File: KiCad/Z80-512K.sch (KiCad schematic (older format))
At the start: 31 parts, among them J1 VBAT, J2 JTAG, J3 RC2014_BUS, J4 RC2014_EXT, U1 Z84C00, U2 SST39SF040, U3 AS6C4008, U4 ATF1504AS, U5 ADM693A, X1 7.3728MHz

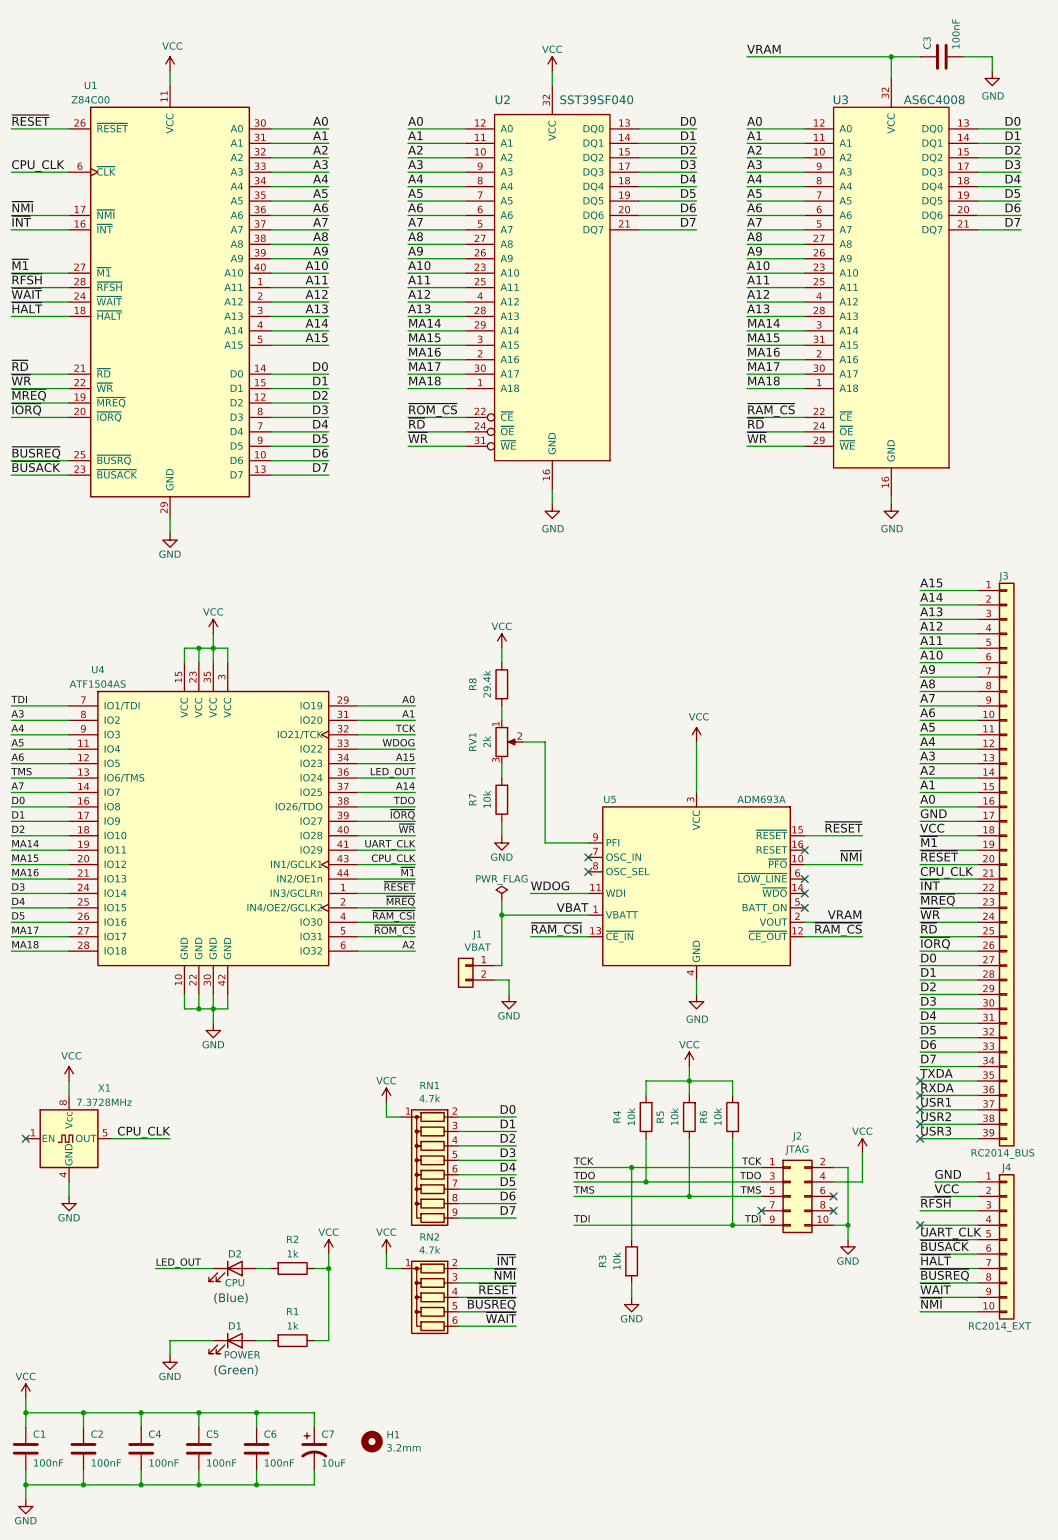
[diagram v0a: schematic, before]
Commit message: Update KiCad, gerber, and README for Version 1.1
Signed-off-by: Sergey Kiselev <skiselev@gmail.com>
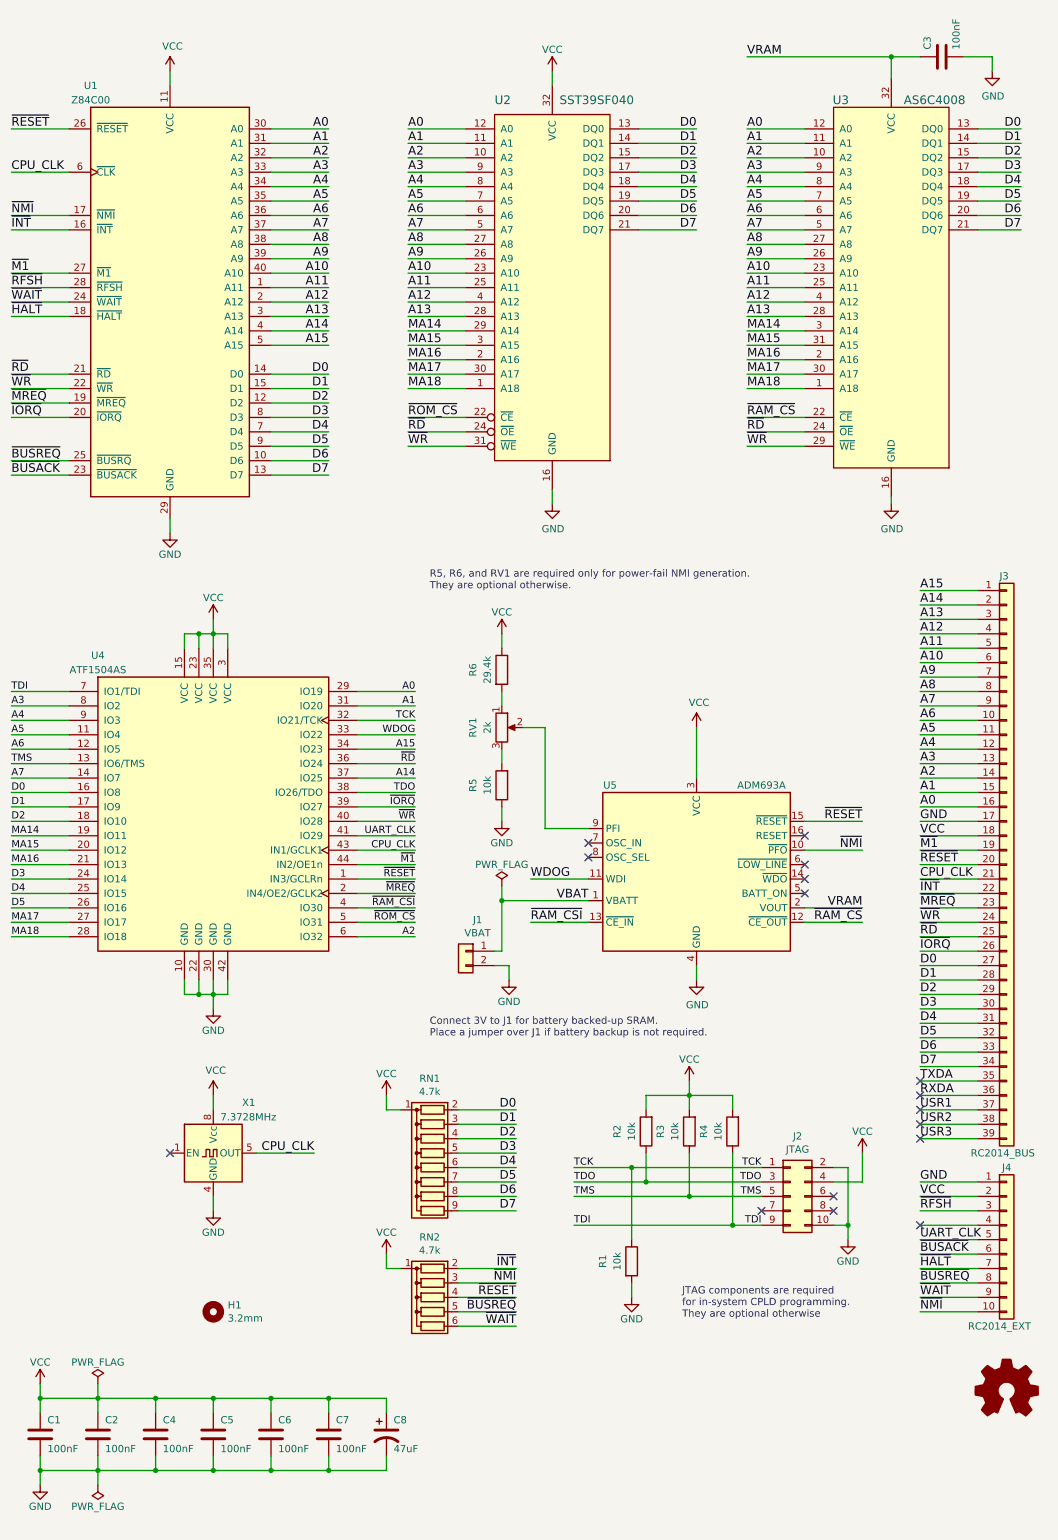
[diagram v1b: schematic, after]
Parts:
- removed D1: POWER, My_Components:LED_3mm, symbol Device:LED
- removed D2: CPU, My_Components:LED_3mm, symbol Device:LED
- removed R1, R2: 1k, Resistor_THT:R_Axial_DIN0204_L3.6mm_D1.6mm_P2.54mm_Vertical, symbol Device:R
- added C7: 100nF, My_Components:Cap_Cer_508, symbol Device:C
- added LOGO1: Logo_Open_Hardware_Small, Symbol:OSHW-Logo_5.7x6mm_SilkScreen, symbol Graphic:Logo_Open_Hardware_Small
- C8: renamed from C7; value 10uF -> 47uF; footprint My_Components:Cap_Cer_508 -> Capacitor_THT:CP_Radial_D5.0mm_P2.00mm
- J3: footprint My_Components:Conn_Pin_Header_39x1_2.54mm -> My_Components:Conn_Pin_Header_39x1_2.54mm_Right_Angle
- J4: footprint My_Components:Conn_Pin_Header_10x1_2.54mm -> My_Components:Conn_Pin_Header_10x1_2.54mm_Right_Angle
- U1: footprint My_Components:IC_DIP40_600 -> My_Components:Socket_DIP40_600
- U2, U3: footprint My_Components:IC_DIP32_600 -> My_Components:Socket_DIP32_600
- U5: footprint My_Components:IC_DIP16_300 -> My_Components:Socket_DIP16_300
- renumbered R3 to R1, R4 to R2, R5 to R3, R6 to R4, R7 to R5, R8 to R6
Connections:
- net LED_OUT is gone; now on net ~RD: U4.36 (IO24)
- net GND: now also C7.2
- net VCC: now also C7.1
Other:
- note added: "Connect 3V to J1 for battery backed-up SRAM.\nPlace a jumper over J1 if battery backup is not required."
- note added: "JTAG components are required\nfor in-system CPLD programming.\nThey are optional otherwise"
- note added: "R5, R6, and RV1 are required only for power-fail NMI generation.\nThey are optional otherwise."
- note removed: "(Blue)"
- note removed: "(Green)"
- moved on the sheet: C1, C2, C4, C5, C6, C8, H1, J1, R2, R3, R4, R5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

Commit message: Replace design files with version 1.2. Update README accordingly
Signed-off-by: Sergey Kiselev <skiselev@gmail.com>
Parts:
- added D1: CPU, My_Components:LED_3mm, symbol Device:LED
- added R7: 1k, Resistor_THT:R_Axial_DIN0204_L3.6mm_D1.6mm_P2.54mm_Vertical, symbol Device:R
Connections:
- net VCC: now also R7.1
- net WDOG: now also D1.1 (K)
- new net: D1.2 (A), R7.2
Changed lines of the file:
@@
 Sheet 1 1
 Title "Z80-512K: RC2014 Compatible CPU and Memory Module"
-Date "2021-01-15"
-Rev "1.1"
+Date "2021-01-25"
+Rev "1.2"
 Comp "Designed by Sergey Kiselev"
 Comment1 ""
@@
 Wire Wire Line
 	6100 7000 6500 7000
-Text Label 4200 6700 0    60   ~ 0
-WDOG
 Text Label 4200 7000 0    60   ~ 0
 ~RAM_CSI
@@
 $EndComp
 Wire Wire Line
-	4600 6700 4200 6700
+	4600 6700 4500 6700
 Wire Wire Line
 	4000 6750 4000 6850
@@
 Text Notes 5250 9750 0    50   ~ 0
 JTAG components are required\nfor in-system CPLD programming.\nThey are optional otherwise
+$Comp
+L Device:LED D1
+U 1 1 60106816
+P 4500 5650
+F 0 "D1" V 4539 5532 50  0000 R CNN
+F 1 "CPU" V 4448 5532 50  0000 R CNN
+F 2 "My_Components:LED_3mm" H 4500 5650 50  0001 C CNN
+F 3 "~" H 4500 5650 50  0001 C CNN
+	1    4500 5650
+	0    -1   -1   0
+$EndComp
+Wire Wire Line
+	4500 5400 4500 5500
+$Comp
+L power:VCC #PWR0107
+U 1 1 601691CF
+P 4500 5000
+F 0 "#PWR0107" H 4500 4850 50  0001 C CNN
+F 1 "VCC" H 4500 5150 50  0000 C CNN
+F 2 "" H 4500 5000 50  0001 C CNN
+F 3 "" H 4500 5000 50  0001 C CNN
+	1    4500 5000
+	1    0    0    -1
+$EndComp
+Wire Wire Line
+	4500 5000 4500 5100
+Wire Wire Line
+	4500 5800 4500 6700
+Connection ~ 4500 6700
+Wire Wire Line
+	4500 6700 4200 6700
+Text Label 4200 6700 0    60   ~ 0
+WDOG
+$Comp
+L Device:R R7
+U 1 1 601085EA
+P 4500 5250
+F 0 "R7" V 4300 5250 50  0000 C CNN
+F 1 "1k" V 4400 5250 50  0000 C CNN
+F 2 "Resistor_THT:R_Axial_DIN0204_L3.6mm_D1.6mm_P2.54mm_Vertical" V 4430 5250 50  0001 C CNN
+F 3 "" H 4500 5250 50  0001 C CNN
+	1    4500 5250
+	1    0    0    -1
+$EndComp
 $EndSCHEMATC

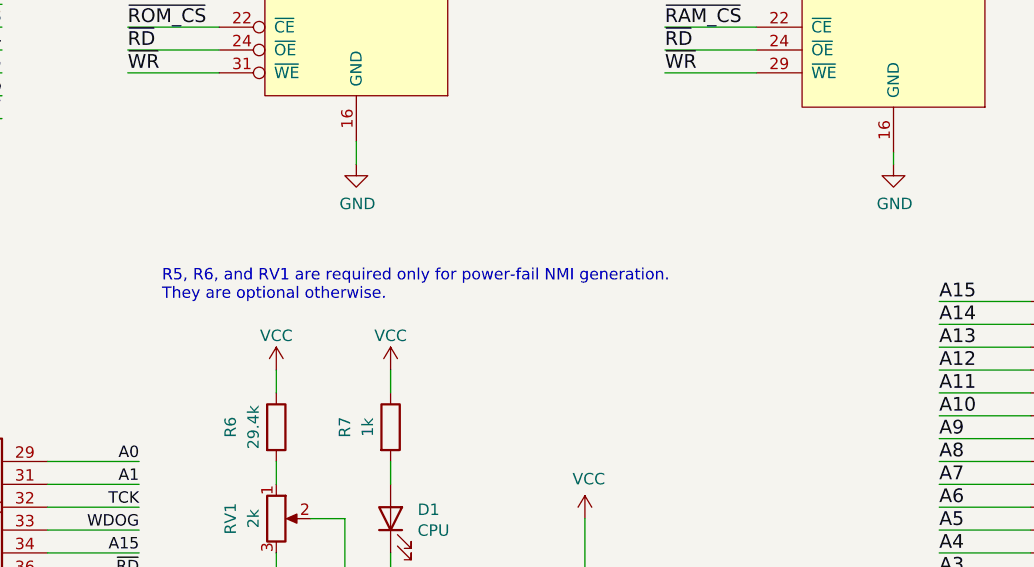
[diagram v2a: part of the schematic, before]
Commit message: KiCad: Remove comment about power fail components
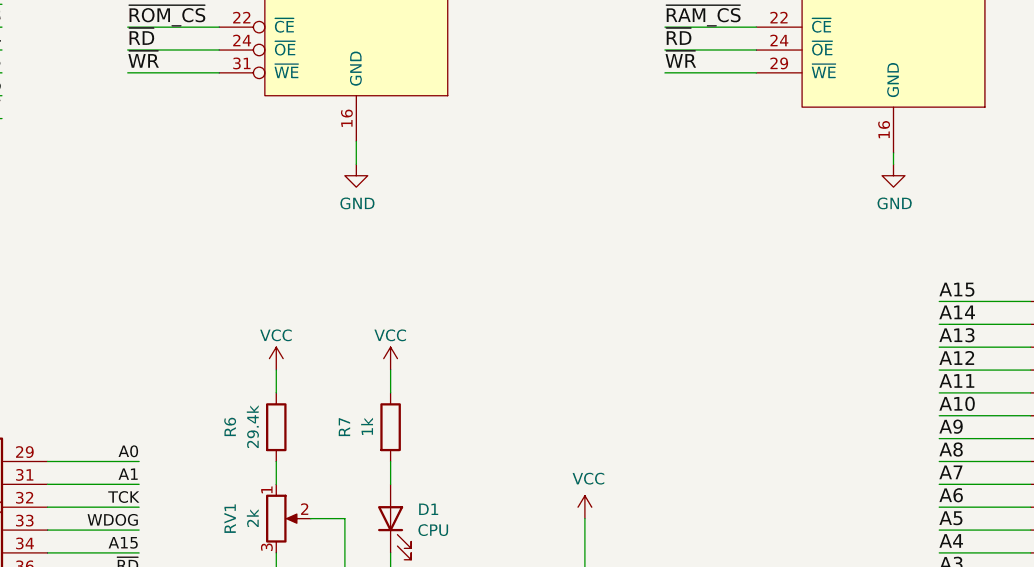
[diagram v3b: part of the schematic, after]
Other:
- note removed: "R5, R6, and RV1 are required only for power-fail NMI generation.\nThey are optional otherwise."
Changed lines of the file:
@@
 Text Notes 3500 7800 0    50   ~ 0
 Connect 3V to J1 for battery backed-up SRAM.\nPlace a jumper over J1 if battery backup is not required.
-Text Notes 3500 4700 0    50   ~ 0
-R5, R6, and RV1 are required only for power-fail NMI generation.\nThey are optional otherwise.
 Wire Wire Line
 	2800 10800 3200 10800
